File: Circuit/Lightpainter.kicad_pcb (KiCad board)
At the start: 2 copper layers, 10 parts, among them K1 CONN_3, SW1 SW_PUSH, SW2 SW_PUSH, U1 78L05, U2 Arduino_Nano_v3, U3 SD_Card_Socket

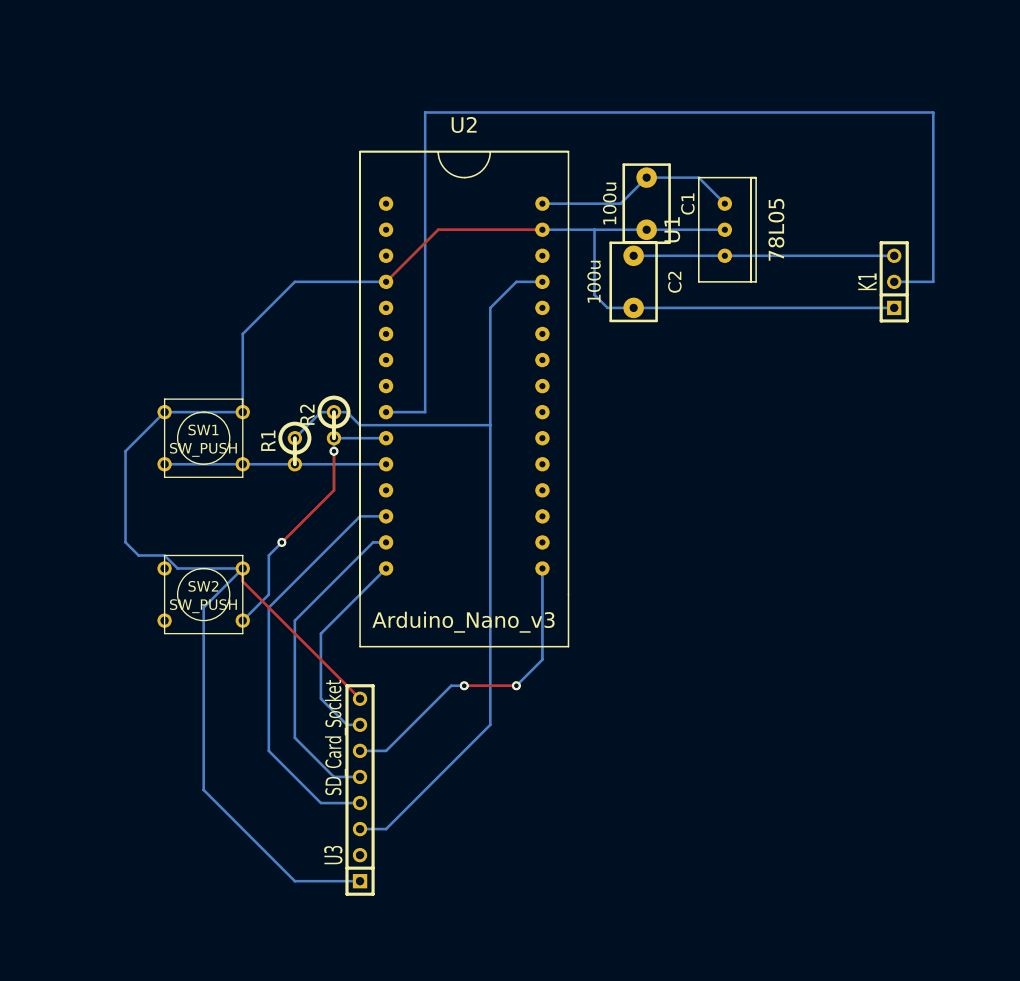
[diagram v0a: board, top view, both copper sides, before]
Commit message: Added 'PCB'
which is actually a layout idea for using veroboard
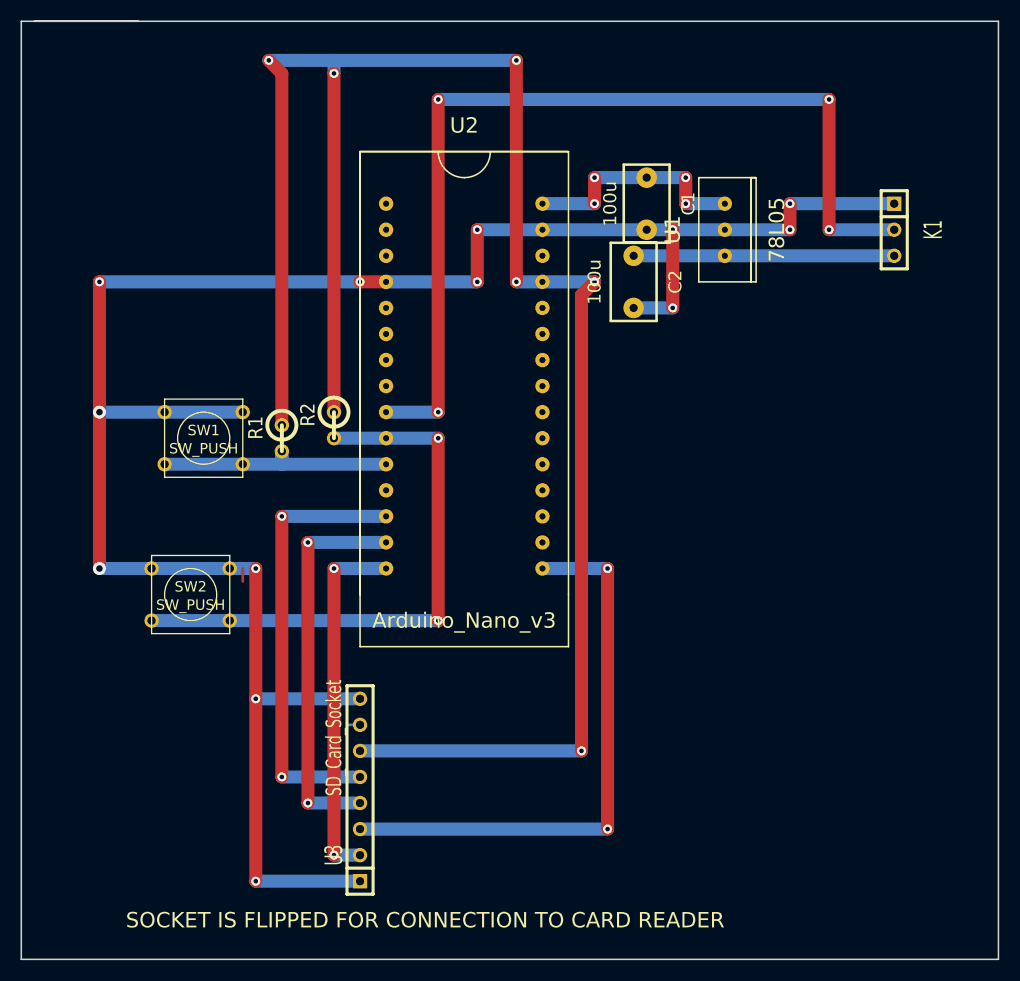
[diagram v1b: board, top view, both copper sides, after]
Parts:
- moved K1 5.08 mm to (219.7, 50.8), turned to 270 degrees
- moved R1 1.80 mm to (160.0, 71.1)
- moved SW2 1.27 mm to (151.1, 86.4)
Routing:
- net +5V: track 84.3 -> 191.6 mm, vias 0 -> 6
- net Net-(R2-Pad2): track 26.5 -> 55.9 mm, vias 2 -> 3
- net Net-(U2-Pad16): track 30.4 -> 55.9 mm
- net GND: track 188.8 -> 204.5 mm, vias 2 -> 17
- net Net-(U2-Pad15): track 20.2 -> 35.6 mm, vias 0 -> 2
- net STRIP_DATA: track 102.9 -> 92.7 mm, vias 0 -> 4
- net Net-(U2-Pad14): track 31.4 -> 38.1 mm, vias 0 -> 2
- net Net-(U2-Pad13): track 40.1 -> 43.2 mm, vias 0 -> 2
- net VDD: track 19.9 -> 22.9 mm, vias 0 -> 4
- net Net-(R1-Pad2): track 21.6 -> 24.1 mm
- net (no net): track 0.00 -> 1.27 mm
- net Net-(U3-Pad2): track 0.00 -> 1.27 mm
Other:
- board outline added: 95.2 x 91.4 mm
- net class AllConns added: clearance 0.254, trace_width 1.27, via_dia 0.889, via_drill 0.635
